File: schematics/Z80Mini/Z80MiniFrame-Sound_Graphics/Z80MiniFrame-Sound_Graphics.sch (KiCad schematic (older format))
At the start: 3 parts, among them J1 Conn_02x20_Odd_Even, U13 74LS139

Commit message: Latest modifications
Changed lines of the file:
@@
 	4950 2600 1700 2600
 Wire Wire Line
-	2400 5300 4400 5300
+	2400 5300 4200 5300
 Wire Wire Line
-	4400 5300 4400 4100
+	4200 5300 4200 4100
 Wire Wire Line
-	4400 4100 5050 4100
+	2400 6100 4500 6100
 Wire Wire Line
-	2400 6100 4900 6100
-Wire Wire Line
-	4900 6100 4900 4550
-Wire Wire Line
-	4900 4550 5050 4550
+	4500 6100 4500 4550
 Wire Wire Line
 	5050 4250 2950 4250
 Wire Wire Line
 	2950 4250 2950 4700
-Wire Wire Line
-	2400 5200 4800 5200
-Wire Wire Line
-	4800 5200 4800 4400
-Wire Wire Line
-	4800 4400 5050 4400
 $Comp
 L 74xx_IEEE:74LS139 U13
@@
 Wire Wire Line
 	6600 4750 5950 4750
-Wire Wire Line
-	5000 6100 4900 6100
-Connection ~ 4900 6100
 Wire Wire Line
 	5000 5750 2700 5750
@@
 NoConn ~ 1900 6300
 Wire Wire Line
+	4300 5200 4300 4400
+Wire Wire Line
+	2400 5200 4300 5200
+Wire Wire Line
+	4300 4400 5050 4400
+Connection ~ 4500 6100
+Wire Wire Line
+	4500 6100 5000 6100
+Wire Wire Line
+	4500 4550 5050 4550
+Wire Wire Line
+	4200 4100 5050 4100
+Wire Wire Line
 	2400 4700 2950 4700

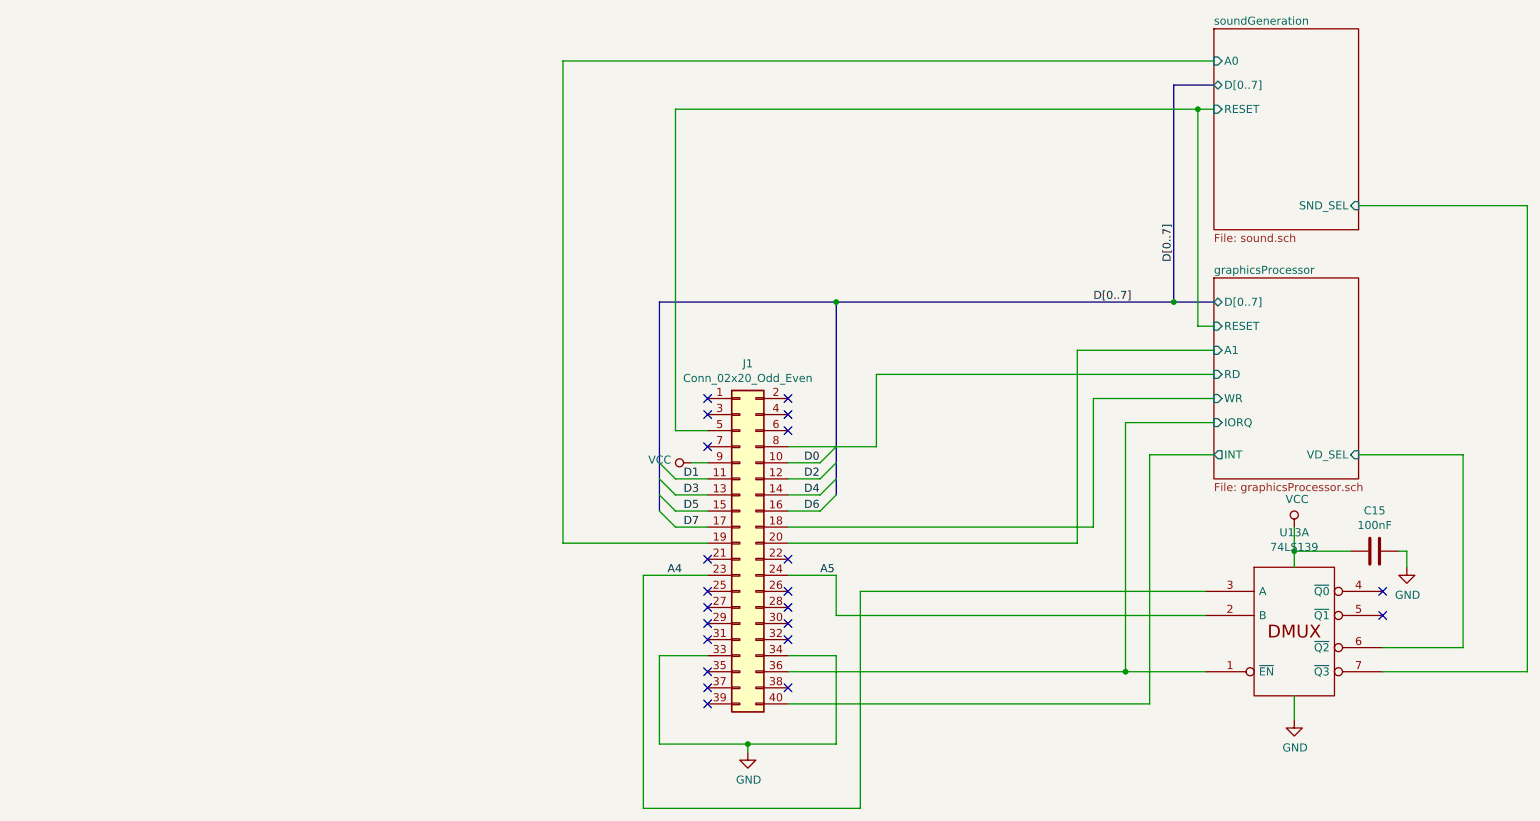
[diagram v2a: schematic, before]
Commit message: Latest modifications and update to v1.1 and first successifully VDP routines test.
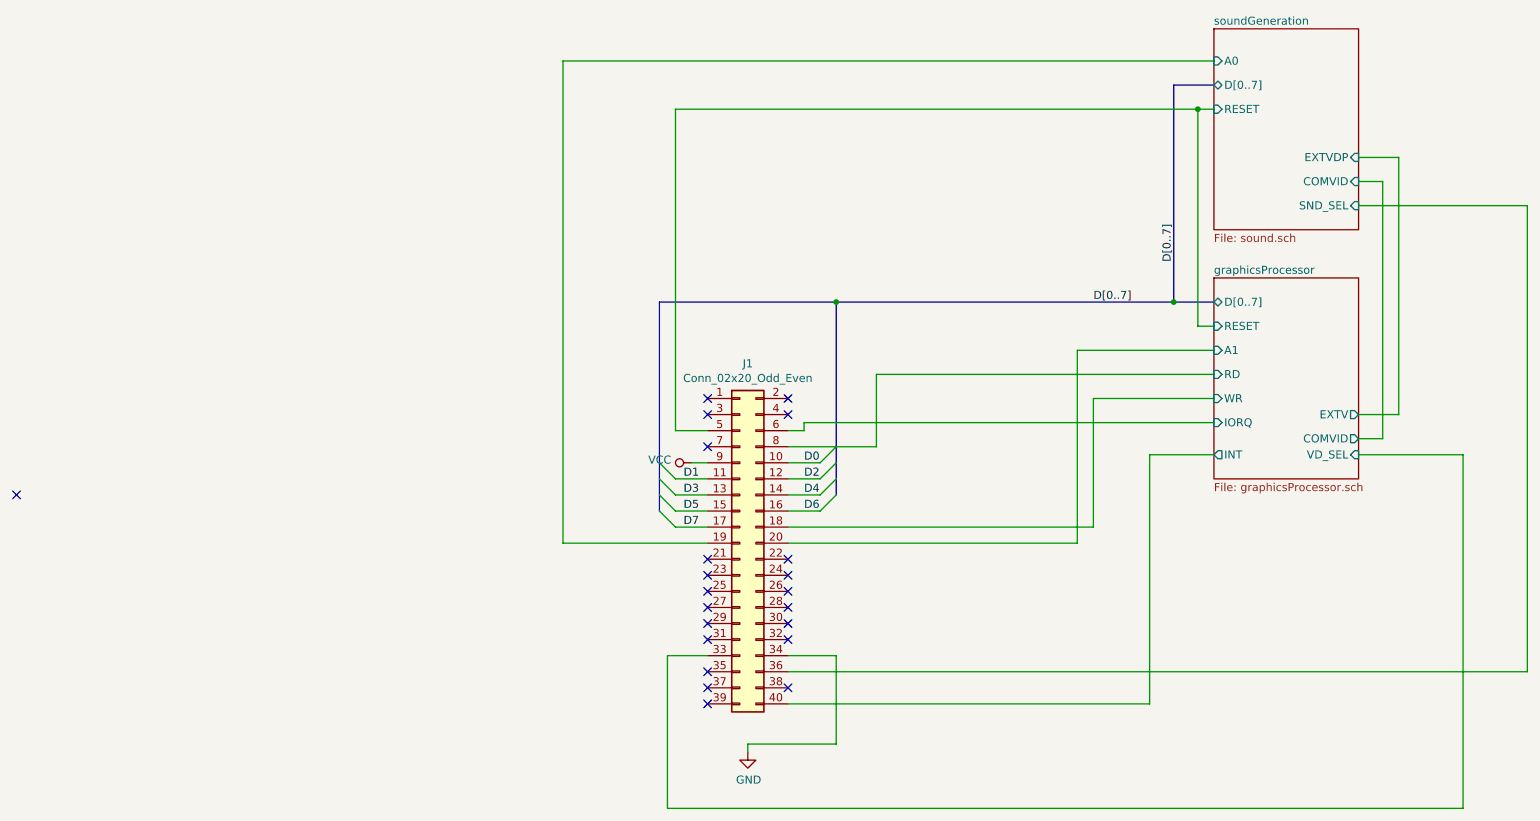
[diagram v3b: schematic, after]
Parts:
- removed C15: 100nF, Capacitor_THT:C_Disc_D7.0mm_W2.5mm_P5.00mm, symbol Device:C
- removed U13: 74LS139, Package_DIP:DIP-16_W7.62mm_LongPads, symbol 74xx_IEEE:74LS139
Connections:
- net GND: no longer J1.33 (Pin_33)
- net graphicsProcessor/IORQ: now also J1.6 (Pin_6); no longer J1.36 (Pin_36)
- net graphicsProcessor/VD_SEL: now also J1.33 (Pin_33)
- net soundGeneration/SND_SEL: now also J1.36 (Pin_36)
- net A4: no longer names the net of J1.23 (Pin_23)
- net A5: no longer names the net of J1.24 (Pin_24)
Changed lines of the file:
@@
 $Descr A4 11693 8268
 encoding utf-8
-Sheet 1 4
+Sheet 1 3
 Title ""
 Date ""
@@
 $EndComp
 Wire Wire Line
-	1900 6000 1600 6000
-Wire Wire Line
-	1600 6000 1600 6550
-Wire Wire Line
-	1600 6550 2150 6550
-Wire Wire Line
 	2700 6550 2700 6000
 Wire Wire Line
@@
 Wire Wire Line
 	2150 6600 2150 6550
-Connection ~ 2150 6550
 Wire Wire Line
 	2150 6550 2700 6550
@@
 F8 "VD_SEL" I R 5950 4750 50
 F9 "INT" O L 5050 4750 50
+F10 "EXTV" O R 5950 4500 50
+F11 "COMVID" O R 5950 4650 50
 $EndSheet
 $Sheet
@@
 F4 "A0" I L 5050 2300 50
 F5 "SND_SEL" I R 5950 3200 50
+F6 "COMVID" I R 5950 3050 50
+F7 "EXTVDP" I R 5950 2900 50
 $EndSheet
 Wire Wire Line
@@
 	4200 5300 4200 4100
 Wire Wire Line
-	2400 6100 4500 6100
-Wire Wire Line
-	4500 6100 4500 4550
-Wire Wire Line
 	5050 4250 2950 4250
 Wire Wire Line
 	2950 4250 2950 4700
-$Comp
-L 74xx_IEEE:74LS139 U13
-U 1 1 5DE6E254
-P 5550 5850
-F 0 "U13" H 5550 6466 50  0000 C CNN
-F 1 "74LS139" H 5550 6375 50  0000 C CNN
-F 2 "Package_DIP:DIP-16_W7.62mm_LongPads" H 5550 5850 50  0001 C CNN
-F 3 "" H 5550 5850 50  0001 C CNN
-	1    5550 5850
-	1    0    0    -1
-$EndComp
 Wire Wire Line
 	7000 3200 5950 3200
 Wire Wire Line
-	6100 5950 6600 5950
-Wire Wire Line
-	6100 6100 7000 6100
-Wire Wire Line
-	7000 3200 7000 6100
-Wire Wire Line
-	6600 4750 6600 5950
-Wire Wire Line
 	6600 4750 5950 4750
-Wire Wire Line
-	5000 5750 2700 5750
-Wire Wire Line
-	2700 5750 2700 5500
-Wire Wire Line
-	2700 5500 2400 5500
-Text Label 2600 5500 0    50   ~ 0
-A5
-Wire Wire Line
-	5000 5600 2850 5600
-Wire Wire Line
-	2850 5600 2850 6950
-Wire Wire Line
-	2850 6950 1500 6950
-Wire Wire Line
-	1500 6950 1500 5500
-Wire Wire Line
-	1500 5500 1900 5500
-Text Label 1650 5500 0    50   ~ 0
-A4
-NoConn ~ 6100 5600
-NoConn ~ 6100 5750
-$Comp
-L power:GND #PWR0129
-U 1 1 5DE7B514
-P 5550 6400
-F 0 "#PWR0129" H 5550 6150 50  0001 C CNN
-F 1 "GND" H 5555 6227 50  0000 C CNN
-F 2 "" H 5550 6400 50  0001 C CNN
-F 3 "" H 5550 6400 50  0001 C CNN
-	1    5550 6400
-	1    0    0    -1
-$EndComp
-Wire Wire Line
-	5550 6250 5550 6400
-$Comp
-L Device:C C15
-U 1 1 5DE887F1
-P 6050 5350
-AR Path="/5DE887F1" Ref="C15"  Part="1"
-AR Path="/5D76ACBB/5DE887F1" Ref="C?"  Part="1"
-AR Path="/5D79B46A/5DE887F1" Ref="C?"  Part="1"
-F 0 "C15" V 5798 5350 50  0000 C CNN
-F 1 "100nF" V 5889 5350 50  0000 C CNN
-F 2 "Capacitor_THT:C_Disc_D7.0mm_W2.5mm_P5.00mm" H 6088 5200 50  0001 C CNN
-F 3 "~" H 6050 5350 50  0001 C CNN
-	1    6050 5350
-	0    -1   1    0
-$EndComp
-$Comp
-L power:GND #PWR0131
-U 1 1 5DE8D599
-P 6250 5450
-F 0 "#PWR0131" H 6250 5200 50  0001 C CNN
-F 1 "GND" H 6255 5277 50  0000 C CNN
-F 2 "" H 6250 5450 50  0001 C CNN
-F 3 "" H 6250 5450 50  0001 C CNN
-	1    6250 5450
-	1    0    0    -1
-$EndComp
-Wire Wire Line
-	6250 5450 6250 5350
-Wire Wire Line
-	6250 5350 6200 5350
-Wire Wire Line
-	5900 5350 5550 5350
-Connection ~ 5550 5350
-Wire Wire Line
-	5550 5350 5550 5450
-$Comp
-L power:VCC #PWR0130
-U 1 1 5DE91962
-P 5550 5200
-F 0 "#PWR0130" H 5550 5050 50  0001 C CNN
-F 1 "VCC" H 5567 5373 50  0000 C CNN
-F 2 "" H 5550 5200 50  0001 C CNN
-F 3 "" H 5550 5200 50  0001 C CNN
-	1    5550 5200
-	1    0    0    -1
-$EndComp
-Wire Wire Line
-	5550 5200 5550 5350
 Wire Wire Line
 	5050 4750 4650 4750
@@
 NoConn ~ 2400 5600
 NoConn ~ 2400 5400
-NoConn ~ 2400 4600
 NoConn ~ 2400 4500
 NoConn ~ 2400 4400
@@
 Wire Wire Line
 	4300 4400 5050 4400
-Connection ~ 4500 6100
-Wire Wire Line
-	4500 6100 5000 6100
-Wire Wire Line
-	4500 4550 5050 4550
 Wire Wire Line
 	4200 4100 5050 4100
+NoConn ~ 2400 5500
+NoConn ~ 1900 5500
+NoConn ~ -2400 5000
+Wire Wire Line
+	2500 4550 5050 4550
+Wire Wire Line
+	2500 4550 2500 4600
+Wire Wire Line
+	2500 4600 2400 4600
+Wire Wire Line
+	6600 4750 6600 6950
+Wire Wire Line
+	6600 6950 1650 6950
+Wire Wire Line
+	1650 6950 1650 6000
+Wire Wire Line
+	1650 6000 1900 6000
+Wire Wire Line
+	2400 6100 7000 6100
+Wire Wire Line
+	7000 6100 7000 3200
+Wire Wire Line
+	5950 3050 6100 3050
+Wire Wire Line
+	6100 3050 6100 4650
+Wire Wire Line
+	6100 4650 5950 4650
+Wire Wire Line
+	5950 4500 6200 4500
+Wire Wire Line
+	6200 4500 6200 2900
+Wire Wire Line
+	6200 2900 5950 2900
 Wire Wire Line
 	2400 4700 2950 4700

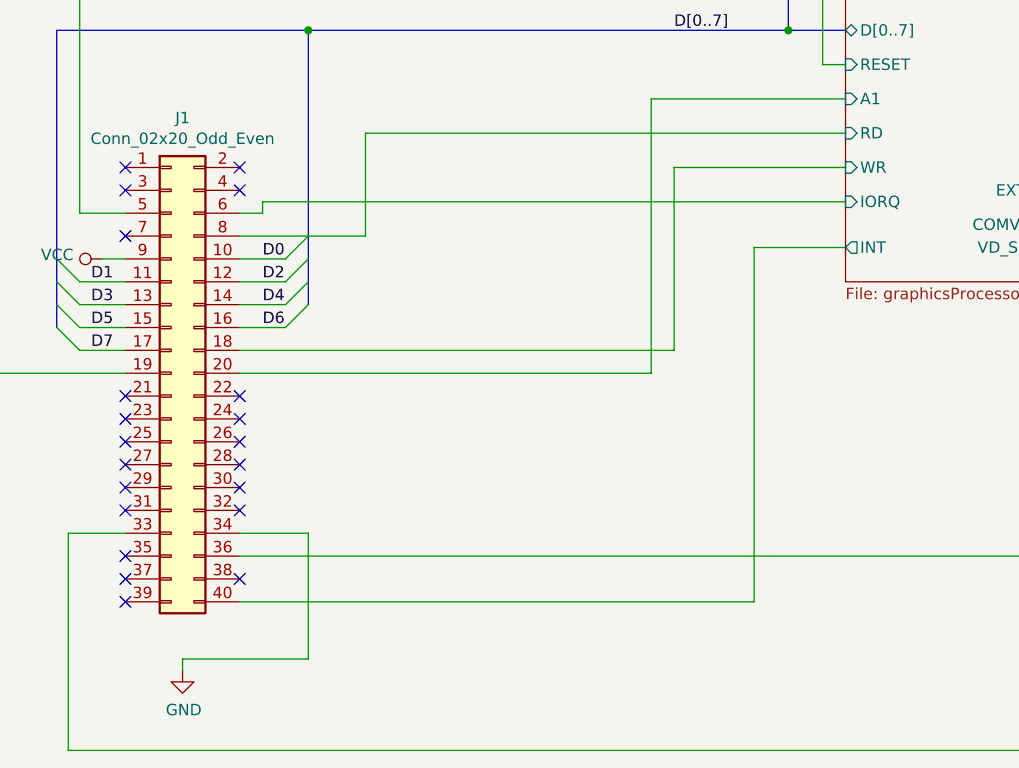
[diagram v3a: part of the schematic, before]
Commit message: Added new code for core written in C with Z88DK
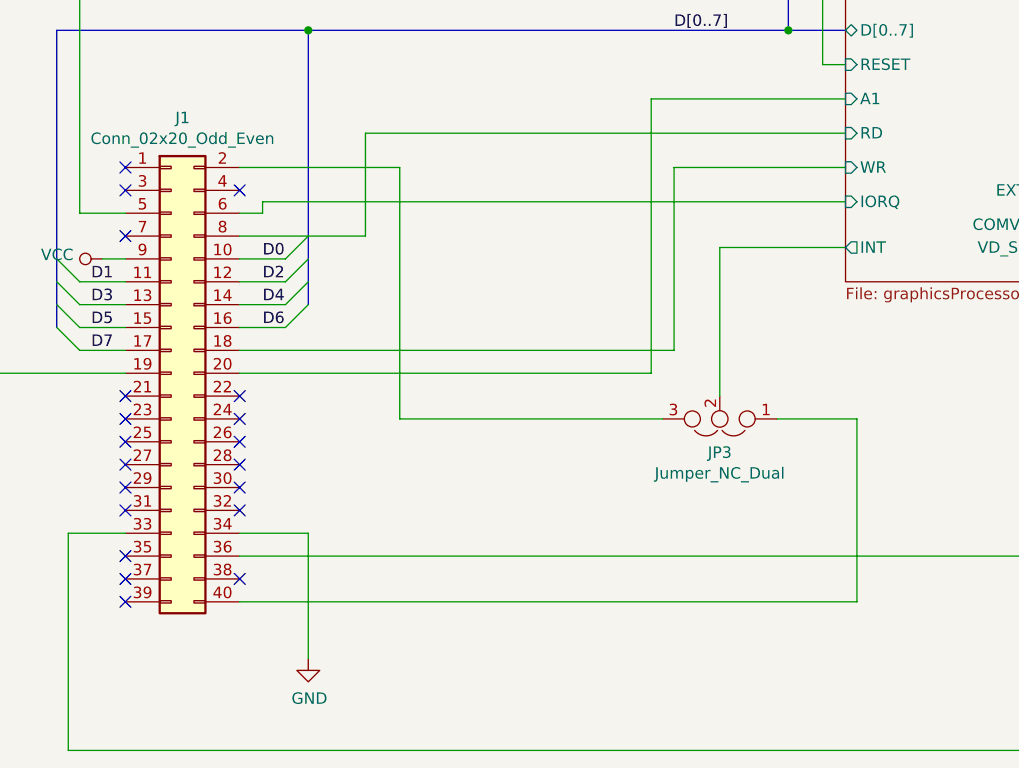
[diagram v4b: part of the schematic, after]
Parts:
- added JP3: Jumper_NC_Dual, Connector_PinHeader_2.00mm:PinHeader_1x03_P2.00mm_Vertical, symbol Device:Jumper_NC_Dual
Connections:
- net graphicsProcessor/INT: now also JP3.2; no longer J1.40 (Pin_40)
- net at J1.2 (Pin_2): now also JP3.3
- new net: J1.40 (Pin_40), JP3.1
- no-connect marks 22 -> 21
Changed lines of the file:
@@
 L power:GND #PWR0102
 U 1 1 5D7227B9
-P 2150 6600
-F 0 "#PWR0102" H 2150 6350 50  0001 C CNN
-F 1 "GND" H 2155 6427 50  0000 C CNN
-F 2 "" H 2150 6600 50  0001 C CNN
-F 3 "" H 2150 6600 50  0001 C CNN
-	1    2150 6600
+P 2700 6550
+F 0 "#PWR0102" H 2700 6300 50  0001 C CNN
+F 1 "GND" H 2705 6377 50  0000 C CNN
+F 2 "" H 2700 6550 50  0001 C CNN
+F 3 "" H 2700 6550 50  0001 C CNN
+	1    2700 6550
 	1    0    0    -1
 $EndComp
-Wire Wire Line
-	2150 6600 2150 6550
-Wire Wire Line
-	2150 6550 2700 6550
 Wire Wire Line
 	1700 4600 1900 4600
@@
 Wire Wire Line
 	6600 4750 5950 4750
-Wire Wire Line
-	5050 4750 4650 4750
-Wire Wire Line
-	4650 4750 4650 6300
-Wire Wire Line
-	4650 6300 2400 6300
 NoConn ~ 2400 6200
 NoConn ~ 2400 5900
@@
 NoConn ~ 2400 5400
 NoConn ~ 2400 4500
-NoConn ~ 2400 4400
 NoConn ~ 1900 4400
 NoConn ~ 1900 4500
@@
 NoConn ~ -2400 5000
 Wire Wire Line
+	6600 4750 6600 6950
+Wire Wire Line
+	6600 6950 1650 6950
+Wire Wire Line
+	1650 6950 1650 6000
+Wire Wire Line
+	1650 6000 1900 6000
+Wire Wire Line
+	2400 6100 7000 6100
+Wire Wire Line
+	7000 6100 7000 3200
+Wire Wire Line
+	5950 3050 6100 3050
+Wire Wire Line
+	6100 3050 6100 4650
+Wire Wire Line
+	6100 4650 5950 4650
+Wire Wire Line
+	5950 4500 6200 4500
+Wire Wire Line
+	6200 4500 6200 2900
+Wire Wire Line
+	6200 2900 5950 2900
+Wire Wire Line
+	2500 4600 2400 4600
+Wire Wire Line
+	2500 4550 2500 4600
+Wire Wire Line
 	2500 4550 5050 4550
 Wire Wire Line
-	2500 4550 2500 4600
-Wire Wire Line
-	2500 4600 2400 4600
-Wire Wire Line
-	6600 4750 6600 6950
-Wire Wire Line
-	6600 6950 1650 6950
-Wire Wire Line
-	1650 6950 1650 6000
-Wire Wire Line
-	1650 6000 1900 6000
-Wire Wire Line
-	2400 6100 7000 6100
-Wire Wire Line
-	7000 6100 7000 3200
-Wire Wire Line
-	5950 3050 6100 3050
-Wire Wire Line
-	6100 3050 6100 4650
-Wire Wire Line
-	6100 4650 5950 4650
-Wire Wire Line
-	5950 4500 6200 4500
-Wire Wire Line
-	6200 4500 6200 2900
-Wire Wire Line
-	6200 2900 5950 2900
+	3100 4400 2400 4400
+$Comp
+L Device:Jumper_NC_Dual JP3
+U 1 1 5DF3C247
+P 4500 5500
+F 0 "JP3" H 4500 5647 50  0000 C CNN
+F 1 "Jumper_NC_Dual" H 4500 5738 50  0000 C CNN
+F 2 "Connector_PinHeader_2.00mm:PinHeader_1x03_P2.00mm_Vertical" H 4500 5500 50  0001 C CNN
+F 3 "~" H 4500 5500 50  0001 C CNN
+	1    4500 5500
+	-1   0    0    1
+$EndComp
+Wire Wire Line
+	3100 5500 4250 5500
+Wire Wire Line
+	3100 4400 3100 5500
+Wire Wire Line
+	4500 5400 4500 4750
+Wire Wire Line
+	4500 4750 5050 4750
+Wire Wire Line
+	4750 5500 5100 5500
+Wire Wire Line
+	5100 5500 5100 6300
+Wire Wire Line
+	5100 6300 2400 6300
 Wire Wire Line
 	2400 4700 2950 4700
